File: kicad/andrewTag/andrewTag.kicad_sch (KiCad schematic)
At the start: 34 parts, among them J1 Micro_SD_Card, P1 USB_C_Plug_USB2.0, SW1 SW_Push, U1 RP2040, U2 W25Q128JVS, U3 L80-R, U4 BQ24074RGT, U5 MCP1700x-330xxTT, Y1 ABM8-272-T3

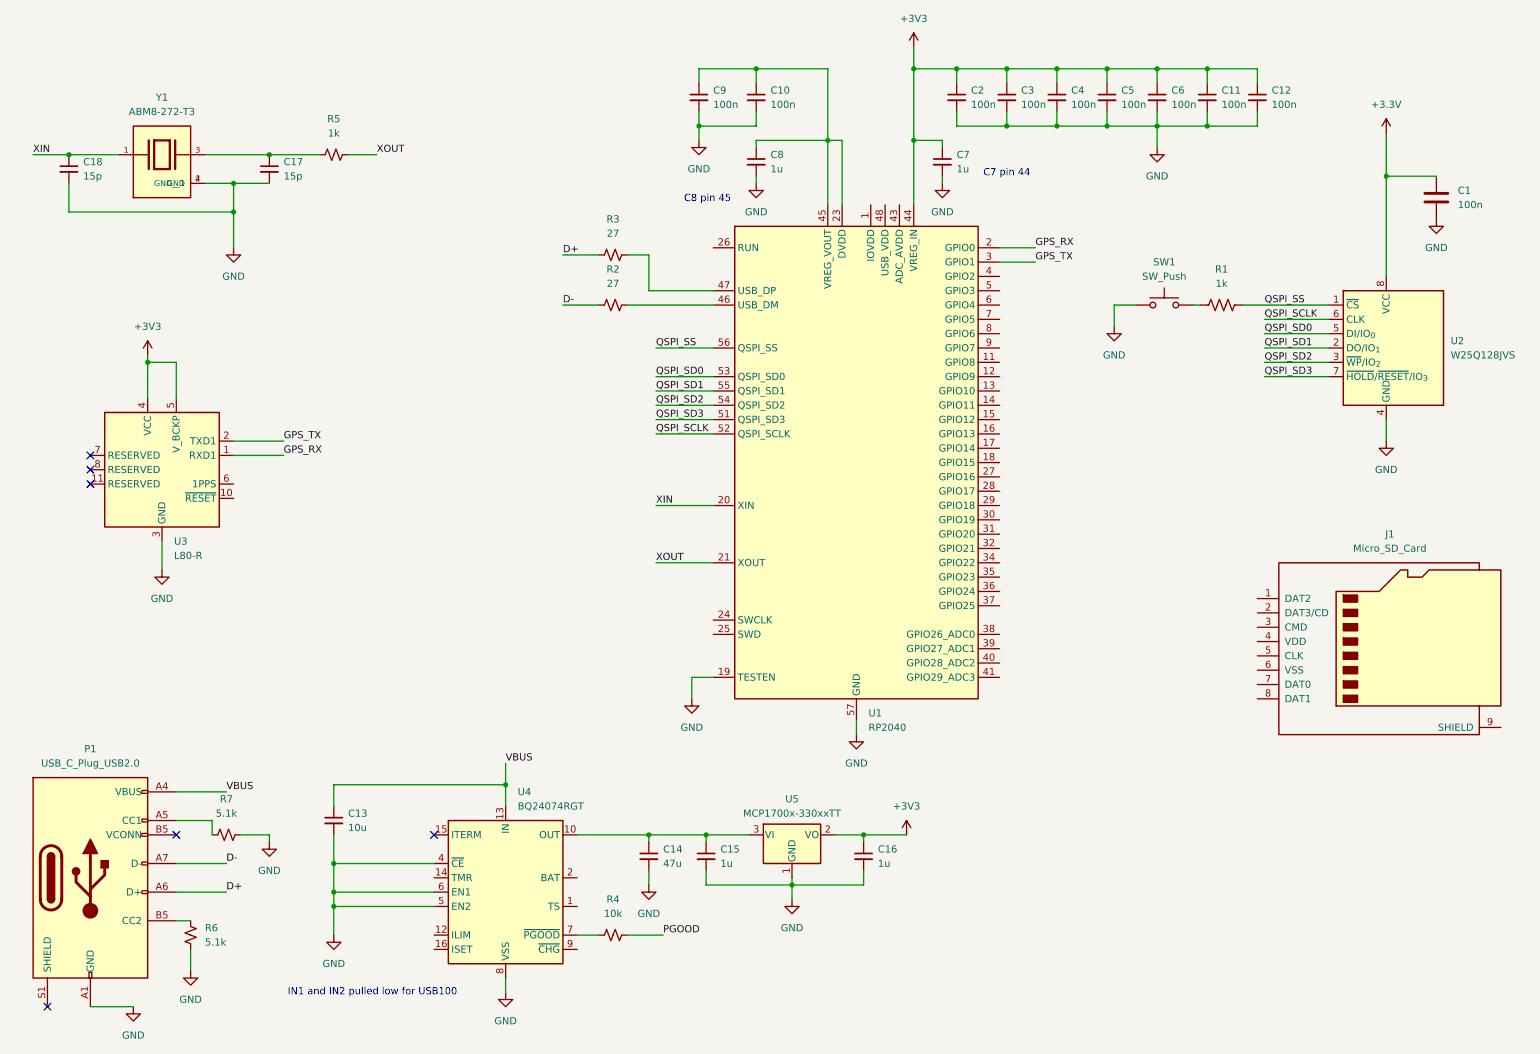
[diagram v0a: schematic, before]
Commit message: replace generic caps with jlc
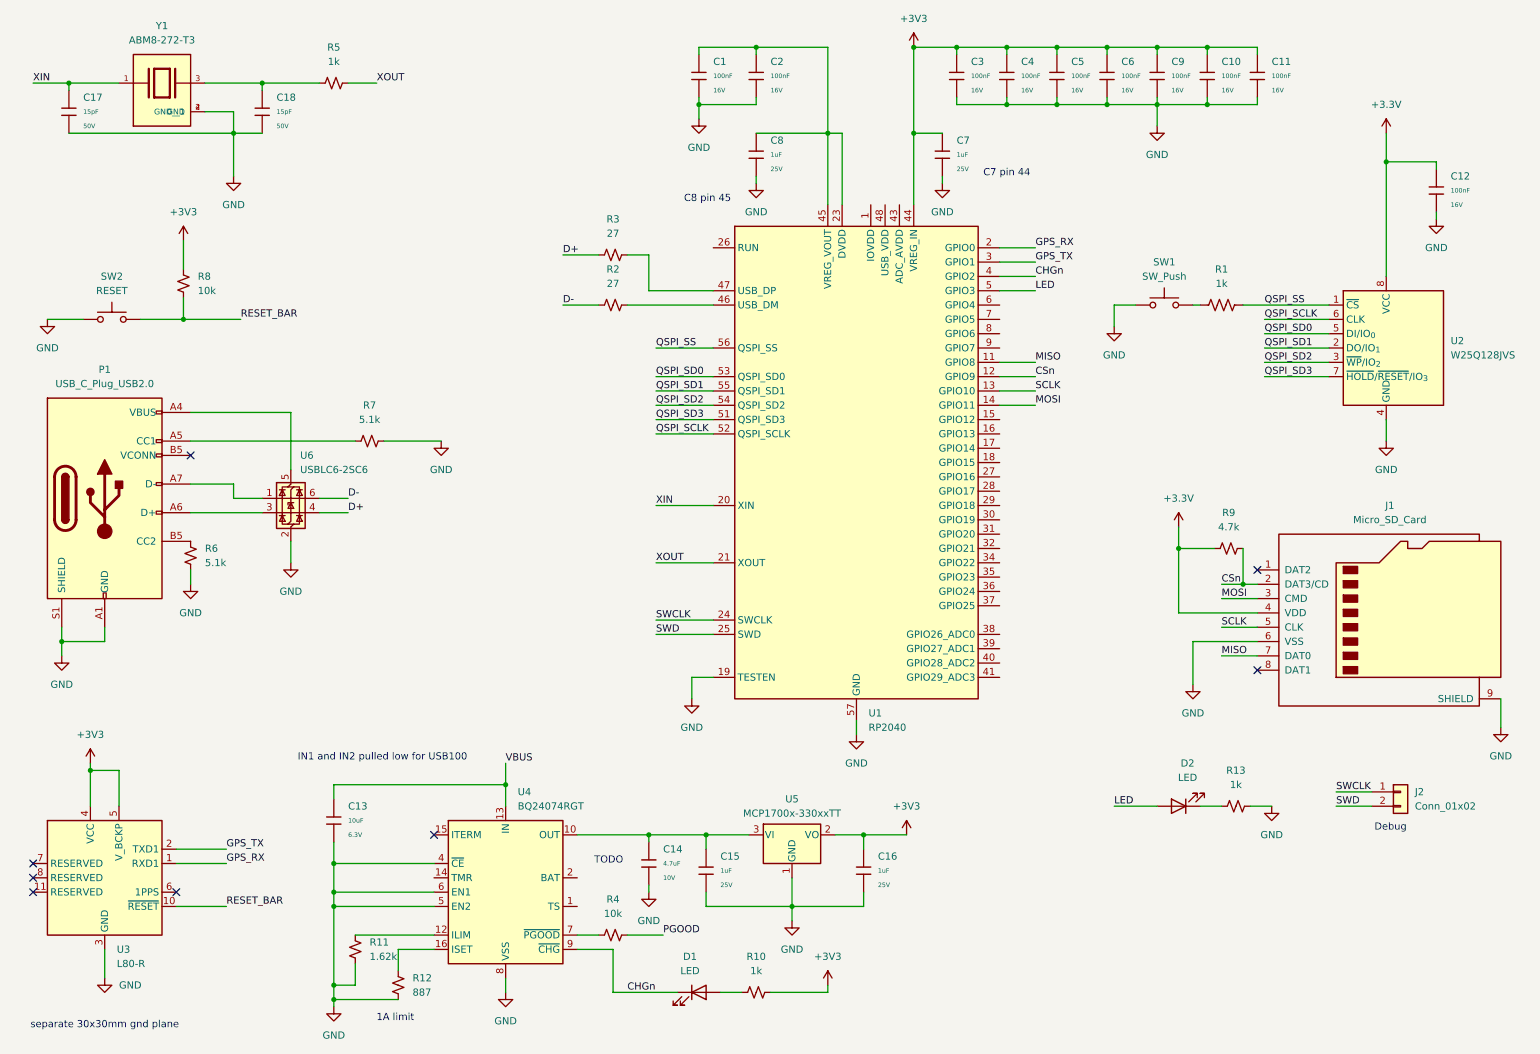
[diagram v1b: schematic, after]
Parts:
- removed C1: 100n, symbol Device:C
- removed C10, C11, C12, C2, C3, C4, C5, C6, C9: 100n, symbol Device:C_Small
- removed C13: 10u, symbol Device:C_Small
- removed C14: 47u, symbol Device:C_Small
- removed C15, C16, C7, C8: 1u, symbol Device:C_Small
- removed C17, C18: 15p, symbol Device:C_Small
- added C1, C10, C11, C12, C2, C3, C4, C5, C6, C9: 100nF, PCM_JLCPCB:C_0402, symbol PCM_JLCPCB-Capacitors:0402,100nF
- added C13: 10uF, PCM_JLCPCB:C_0402, symbol PCM_JLCPCB-Capacitors:0402,10uF
- added C14: 4.7uF, PCM_JLCPCB:C_0402, symbol PCM_JLCPCB-Capacitors:0402,4.7uF
- added C15, C16, C7, C8: 1uF, PCM_JLCPCB:C_0402, symbol PCM_JLCPCB-Capacitors:0402,1uF
- added C17, C18: 15pF, PCM_JLCPCB:C_0402, symbol PCM_JLCPCB-Capacitors:0402,15pF
- added D1, D2: LED, symbol Device:LED
- added J2: Conn_01x02, symbol Connector_Generic:Conn_01x02
- added R10, R13: 1k, symbol Device:R_Small_US
- added R11: 1.62k, symbol Device:R_Small_US
- added R12: 887, symbol Device:R_Small_US
- added R8: 10k, symbol Device:R_Small_US
- added R9: 4.7k, symbol Device:R_Small_US
- added SW2: RESET, symbol Switch:SW_Push
- added U6: USBLC6-2SC6, Package_TO_SOT_SMD:SOT-23-6, symbol Power_Protection:USBLC6-2SC6
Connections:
- net +3.3V: now also J1.4 (VDD), C12.1, R9.2
- net +3V3: now also C10.1, C11.1, C16.1, C3.1, C4.1, C5.1, C6.1, C7.1, C9.1, R10.2, R8.1
- net D+: now also U6.4 (I/O2); no longer P1.A6 (D+)
- net D-: now also U6.6 (I/O1); no longer P1.A7 (D-)
- net GND: now also J1.6 (VSS), J1.9 (SHIELD), P1.S1 (SHIELD), C1.2, C10.2, C11.2, C12.2, C13.2, C14.2, C15.2, C16.2, C17.2, C18.2, C2.2, C3.2, C4.2, C5.2, C6.2, C7.2, C8.2, C9.2, R11.1, R12.1, R13.2, SW2.1, U6.2 (GND)
- net VBUS: now also C13.1; no longer P1.A4 (VBUS), P1.A9 (VBUS), P1.B4 (VBUS), P1.B9 (VBUS)
- net XIN: now also C17.1
- net at U4.10 (OUT), U4.11 (OUT), U5.3 (VI): now also C14.1, C15.1
- net at U1.23 (DVDD), U1.45 (VREG_VOUT), U1.50 (DVDD): now also C1.1, C2.1, C8.1
- net at R5.1, Y1.3: now also C18.1
- net CSn: now reaches J1.2 (DAT3/CD)
- net CSn: now also U1.12 (GPIO9), R9.1
- net MOSI: now reaches J1.3 (CMD)
- net MOSI: now also U1.14 (GPIO11)
- net SCLK: now reaches J1.5 (CLK)
- net SCLK: now also U1.13 (GPIO10)
- net MISO: now reaches J1.7 (DAT0)
- net MISO: now also U1.11 (GPIO8)
- net at P1.B5 (CC2): now also R6.1
- net at U4.12 (ILIM): now also R11.2
- net at U4.16 (ISET): now also R12.2
- net CHGn: now reaches U4.9 (~{CHG})
- net CHGn: now also U1.4 (GPIO2), D1.1 (K)
- net RESET_BAR: now reaches U3.10 (~{RESET})
- net RESET_BAR: now also R8.2, SW2.2
- net SWCLK: now reaches U1.24 (SWCLK)
- net SWCLK: now also J2.1 (Pin_1)
- net SWD: now reaches U1.25 (SWD)
- net SWD: now also J2.2 (Pin_2)
- net LED: now reaches U1.5 (GPIO3)
- net LED: now also D2.2 (A)
- new net: D1.2 (A), R10.1
- new net: P1.A4 (VBUS), P1.A9 (VBUS), P1.B4 (VBUS), P1.B9 (VBUS), U6.5 (VBUS)
- new net: P1.A6 (D+), U6.3 (I/O2)
- new net: P1.A7 (D-), U6.1 (I/O1)
- new net: D2.1 (K), R13.1
- no-connect marks 6 -> 8
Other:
- note added: "1A limit"
- note added: "Debug"
- note added: "TODO"
- note added: "separate 30x30mm gnd plane"
- company: (none) -> panpan designs
- title: (none) -> AndrewTag - Personal GNSS Logger
- moved on the sheet: J1, P1, R5, R6, U3, Y1
